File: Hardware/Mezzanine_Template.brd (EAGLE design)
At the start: 30.5 x 44.5 mm, 6 parts, among them U2 EDISON_CONNECTOR_FULLMOUNTING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, U3 EDISON_CONNECTOR_FULLHEADER

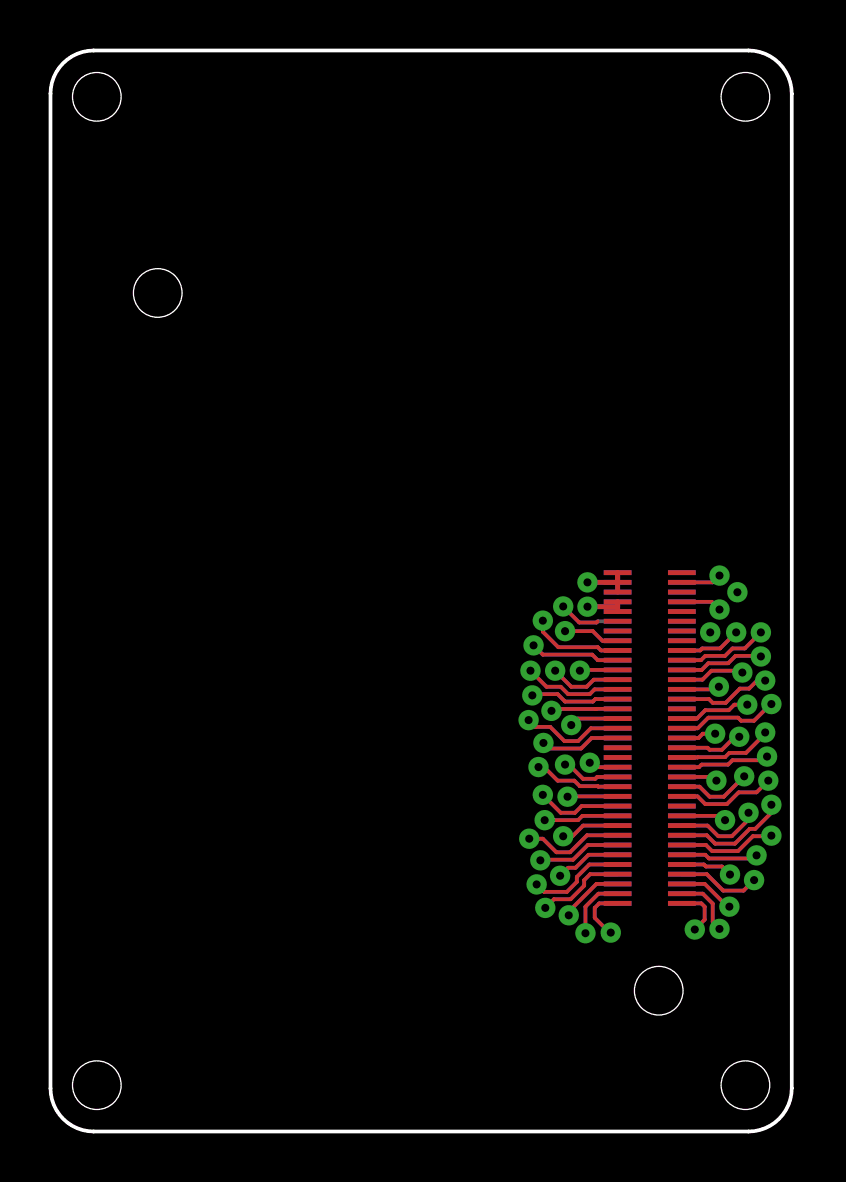
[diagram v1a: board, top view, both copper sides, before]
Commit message: added fiducials and second side logos to template
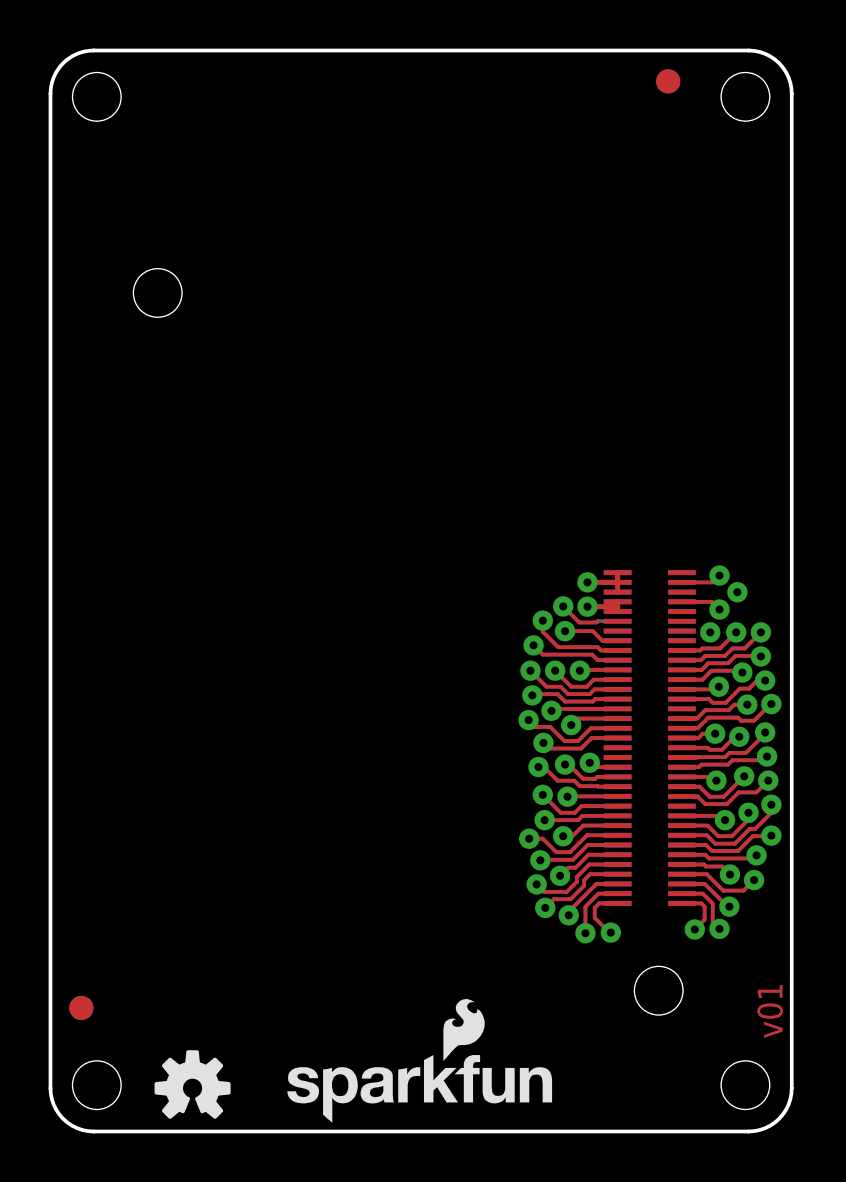
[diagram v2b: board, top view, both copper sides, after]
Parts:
- added FID1, FID2: FIDUCIAL1X2, SparkFun-Aesthetics:FIDUCIAL-1X2
- added LOGO1: OSHW-LOGOS, SparkFun-Aesthetics:OSHW-LOGO-S
- added LOGO4: SFE_LOGO_NAME_FLAME.1_INCH, SparkFun-Aesthetics:SFE_LOGO_NAME_FLAME_.1
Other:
- board text added: "v01"
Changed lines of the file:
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@@
 <dimension x1="29.28210625" y1="41.83789375" x2="27.86789375" y2="43.25210625" x3="34.29" y3="48.26" textsize="1.778" layer="51" dtype="diameter"/>
 <text x="29.21" y="6.35" size="1.016" layer="22" font="vector" ratio="15" rot="MR90" align="center">4xM2.0</text>
+<text x="30.099" y="3.81" size="1.016" layer="1" font="vector" ratio="14" rot="R90">v01</text>
 </plain>
 <attributes>
@@
 <element name="U3" library="Edison" package="DF40C-70DP-0.4(51)" value="EDISON_CONNECTOR_FULLHEADER" x="24.64" y="16.1798" rot="MR90"/>
 <element name="FRAME2" library="SparkFun-Aesthetics" package="CREATIVE_COMMONS" value="FRAME-LETTER" x="-1.27" y="-13.97"/>
+<element name="LOGO1" library="SparkFun-Aesthetics" package="OSHW-LOGO-S" value="OSHW-LOGOS" x="5.842" y="1.778"/>
+<element name="LOGO4" library="SparkFun-Aesthetics" package="SFE_LOGO_NAME_FLAME_.1" value="SFE_LOGO_NAME_FLAME.1_INCH" x="9.2964" y="0.254"/>
+<element name="FID1" library="SparkFun-Aesthetics" package="FIDUCIAL-1X2" value="FIDUCIAL1X2" x="1.27" y="5.08"/>
+<element name="FID2" library="SparkFun-Aesthetics" package="FIDUCIAL-1X2" value="FIDUCIAL1X2" x="25.4" y="43.18"/>
 </elements>
 <signals>
@@
 <contactref element="U2" pad="12"/>
 <contactref element="U3" pad="12"/>
-<wire x1="23.32" y1="20.9798" x2="23.32" y2="20.98" width="0" layer="19" extent="1-16"/>
+<wire x1="23.32" y1="20.98" x2="23.32" y2="20.9798" width="0" layer="19" extent="1-16"/>
 </signal>
 <signal name="FW_RCVR">

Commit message: - Added fiducials to both sides - flipped side name template is on - corrected 1.8v trace that was not connected. - removed my name from the designed by, Replaced with "Engineer" - Added template rev number to SCH.
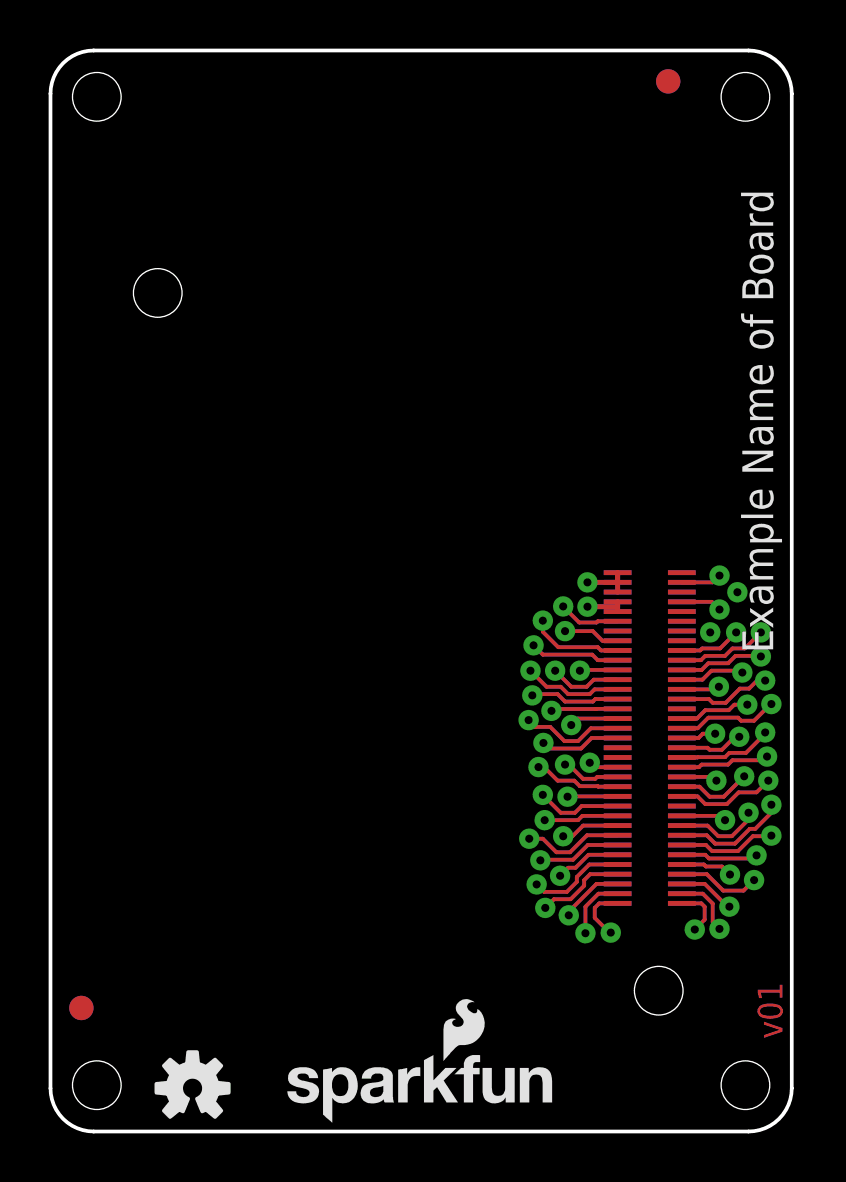
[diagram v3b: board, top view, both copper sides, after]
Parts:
- added FID3, FID4: FIDUCIAL1X2, SparkFun-Aesthetics:FIDUCIAL-1X2
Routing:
- net 1.8V: track 4.25 -> 5.07 mm
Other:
- board text added: "Engineer"
- board text removed: "Casey Kuhns"
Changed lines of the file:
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@@
 <wire x1="28.702" y1="0" x2="1.778" y2="0" width="0.1524" layer="20"/>
 <wire x1="0" y1="1.778" x2="0" y2="42.672" width="0.1524" layer="20"/>
-<text x="27.94" y="-13.97" size="1.6764" layer="51" ratio="15">Casey Kuhns</text>
+<text x="25.4" y="-13.97" size="1.6764" layer="51" ratio="15">Engineer</text>
 <hole x="28.575" y="1.905" drill="2"/>
 <hole x="1.905" y="1.905" drill="2"/>
@@
 <text x="-2.54" y="41.91" size="1.778" layer="51" rot="R270">LED's and selector switches go here</text>
 <text x="31.115" y="39.37" size="1.778" layer="51" rot="R270">Nothing goes here...  I mean it.</text>
-<text x="29.337" y="29.21" size="1.27" layer="22" font="vector" ratio="15" rot="MR90" align="center">Example Name of Board</text>
+<text x="29.083" y="29.21" size="1.27" layer="21" font="vector" ratio="15" rot="R90" align="center">Example Name of Board</text>
 <wire x1="1.778" y1="44.45" x2="28.702" y2="44.45" width="0.1524" layer="20"/>
 <wire x1="30.48" y1="44.704" x2="30.48" y2="53.34" width="0.254" layer="51"/>
@@
 <element name="FID1" library="SparkFun-Aesthetics" package="FIDUCIAL-1X2" value="FIDUCIAL1X2" x="1.27" y="5.08"/>
 <element name="FID2" library="SparkFun-Aesthetics" package="FIDUCIAL-1X2" value="FIDUCIAL1X2" x="25.4" y="43.18"/>
+<element name="FID3" library="SparkFun-Aesthetics" package="FIDUCIAL-1X2" value="FIDUCIAL1X2" x="1.27" y="5.08" rot="MR0"/>
+<element name="FID4" library="SparkFun-Aesthetics" package="FIDUCIAL-1X2" value="FIDUCIAL1X2" x="25.4" y="43.18" rot="MR0"/>
 </elements>
 <signals>
@@
 </signal>
 <signal name="1.8V">
-<wire x1="22.5038" y1="20.9798" x2="22.4536" y2="20.9296" width="0.1524" layer="1"/>
-<wire x1="22.4536" y1="20.9296" x2="21.7424" y2="20.9296" width="0.1524" layer="1"/>
-<wire x1="21.7424" y1="20.9296" x2="21.082" y2="21.59" width="0.1524" layer="1"/>
-<via x="21.082" y="21.59" extent="1-16" drill="0.3302"/>
 <wire x1="21.082" y1="21.59" x2="21.7424" y2="20.9296" width="0.1524" layer="16"/>
 <wire x1="21.7424" y1="20.9296" x2="22.4536" y2="20.9296" width="0.1524" layer="16"/>
@@
 <contactref element="U2" pad="12"/>
 <contactref element="U3" pad="12"/>
-<wire x1="23.32" y1="20.98" x2="23.32" y2="20.9798" width="0" layer="19" extent="1-16"/>
+<via x="21.082" y="21.59" extent="1-16" drill="0.3302"/>
+<wire x1="21.082" y1="21.59" x2="21.7424" y2="20.9296" width="0.1524" layer="1"/>
+<wire x1="21.7424" y1="20.9296" x2="22.4536" y2="20.9296" width="0.1524" layer="1"/>
+<wire x1="22.4536" y1="20.9296" x2="22.5044" y2="20.9804" width="0.1524" layer="1"/>
+<wire x1="22.5044" y1="20.9804" x2="23.3194" y2="20.9804" width="0.1524" layer="1"/>
+<wire x1="23.3194" y1="20.9804" x2="23.32" y2="20.9798" width="0.1524" layer="1"/>
 </signal>
 <signal name="FW_RCVR">

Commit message: corrected lables and removed extra packages that are no longer supported.
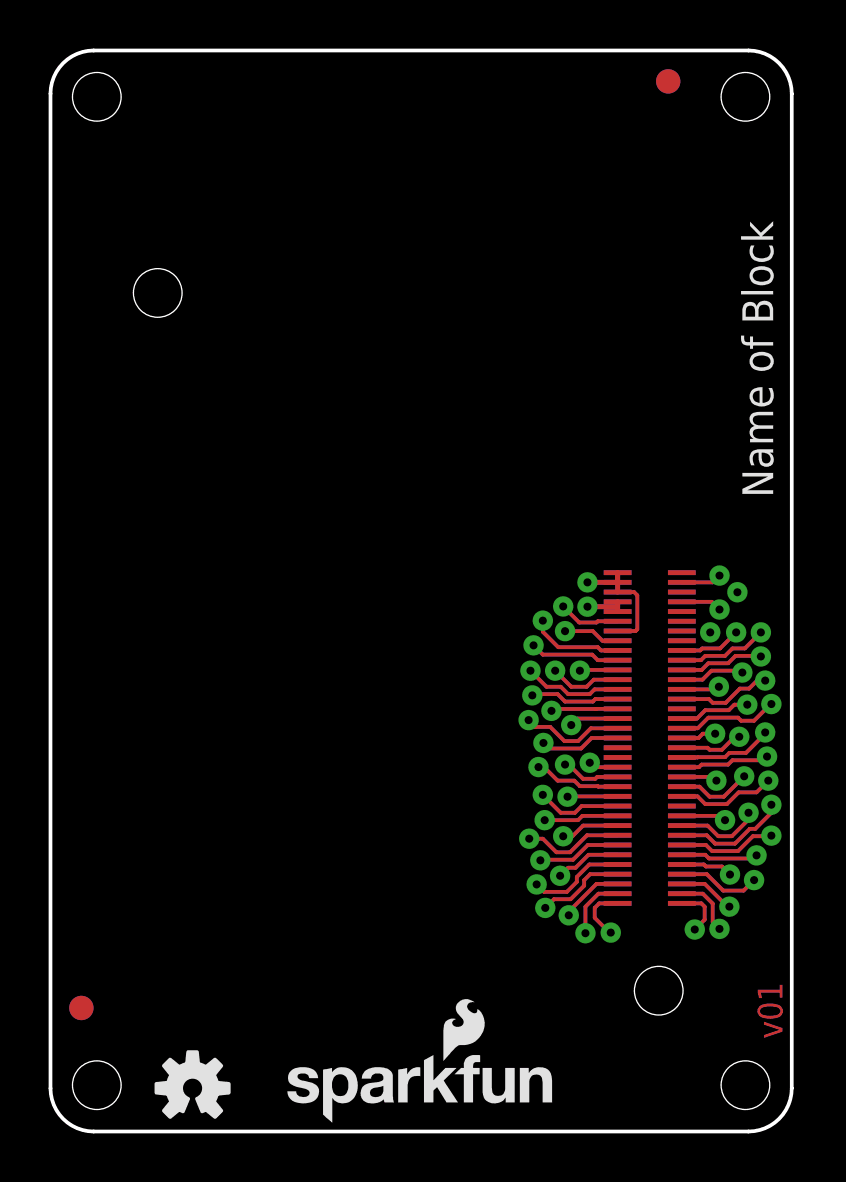
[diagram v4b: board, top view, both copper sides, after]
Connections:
- net VSYS: now also U2.14, U3.14
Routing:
- net VSYS: track 4.48 -> 10.7 mm
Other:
- board text added: "LED's & User Switches/Buttons Go Here"
- board text added: "Name of Block"
- board text added: "Note: Units are in Inches"
- board text added: "User Interface/ Connectors"
- board text removed: "Connectors Go Here"
- board text removed: "Example Name of Board"
- board text removed: "LED's and selector switches go here"
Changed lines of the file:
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@@
 <?xml version="1.0" encoding="utf-8"?>
 <!DOCTYPE eagle SYSTEM "eagle.dtd">
-<eagle version="6.5.0">
+<eagle version="6.6.0">
 <drawing>
 <settings>
@@
 <setting verticaltext="up"/>
 </settings>
-<grid distance="0.05" unitdist="inch" unit="inch" style="lines" multiple="1" display="yes" altdistance="0.005" altunitdist="inch" altunit="inch"/>
+<grid distance="0.001" unitdist="inch" unit="inch" style="lines" multiple="1" display="yes" altdistance="0.005" altunitdist="inch" altunit="inch"/>
 <layers>
 <layer number="1" name="Top" color="4" fill="1" visible="yes" active="yes"/>
@@
 <layer number="20" name="Dimension" color="15" fill="1" visible="yes" active="yes"/>
 <layer number="21" name="tPlace" color="16" fill="1" visible="yes" active="yes"/>
-<layer number="22" name="bPlace" color="14" fill="1" visible="yes" active="yes"/>
+<layer number="22" name="bPlace" color="14" fill="1" visible="no" active="yes"/>
 <layer number="23" name="tOrigins" color="15" fill="1" visible="yes" active="yes"/>
 <layer number="24" name="bOrigins" color="15" fill="1" visible="yes" active="yes"/>
@@
 <hole x="1.905" y="42.545" drill="2"/>
 <hole x="28.575" y="42.545" drill="2"/>
-<text x="4.445" y="45.085" size="1.778" layer="51">Connectors Go Here</text>
-<text x="-2.54" y="41.91" size="1.778" layer="51" rot="R270">LED's and selector switches go here</text>
+<text x="8.255" y="45.085" size="1.778" layer="51">User Interface/
+ Connectors</text>
+<text x="-2.54" y="41.91" size="1.778" layer="51" rot="R270">LED's &amp; User Switches/Buttons Go Here</text>
 <text x="31.115" y="39.37" size="1.778" layer="51" rot="R270">Nothing goes here...  I mean it.</text>
-<text x="29.083" y="29.21" size="1.27" layer="21" font="vector" ratio="15" rot="R90" align="center">Example Name of Board</text>
+<text x="29.083" y="31.75" size="1.27" layer="21" font="vector" ratio="15" rot="R90" align="center">Name of Block</text>
 <wire x1="1.778" y1="44.45" x2="28.702" y2="44.45" width="0.1524" layer="20"/>
 <wire x1="30.48" y1="44.704" x2="30.48" y2="53.34" width="0.254" layer="51"/>
@@
 <rectangle x1="22.098" y1="26.162" x2="30.48" y2="44.45" layer="42" rot="R180"/>
 <rectangle x1="22.098" y1="26.162" x2="30.48" y2="44.45" layer="41" rot="R180"/>
-<dimension x1="1.778" y1="42.672" x2="0.4190875" y2="43.81858125" x3="-5.542384375" y3="48.848575" textsize="1.778" layer="51" dtype="radius"/>
+<dimension x1="1.905" y1="42.545" x2="0.4190875" y2="43.81858125" x3="-5.503225" y3="48.894621875" textsize="1.778" layer="51" dtype="radius" unit="inch"/>
 <dimension x1="29.28210625" y1="41.83789375" x2="27.86789375" y2="43.25210625" x3="34.29" y3="48.26" textsize="1.778" layer="51" dtype="diameter"/>
 <text x="29.21" y="6.35" size="1.016" layer="22" font="vector" ratio="15" rot="MR90" align="center">4xM2.0</text>
-<text x="30.099" y="3.81" size="1.016" layer="1" font="vector" ratio="14" rot="R90">v01</text>
+<text x="30.099" y="3.81" size="1.016" layer="1" font="vector" ratio="15" rot="R90">v01</text>
+<text x="33.02" y="-3.81" size="1.778" layer="51">Note: Units are in Inches</text>
+<text x="29.083" y="31.75" size="1.27" layer="22" font="vector" ratio="15" rot="SMR270" align="center">Name of Block</text>
 </plain>
 <attributes>
@@
 <signals>
 <signal name="GND">
-<polygon width="0.1778" layer="16" spacing="0.254" isolate="0.1524" orphans="yes" rank="6">
+<polygon width="0.1778" layer="16" spacing="0.254" orphans="yes" rank="6">
 <vertex x="30.48" y="42.672"/>
 <vertex x="30.48" y="1.778" curve="-90"/>
@@
 <contactref element="U3" pad="2"/>
 <contactref element="U3" pad="4"/>
+<contactref element="U2" pad="14"/>
+<contactref element="U3" pad="14"/>
+<wire x1="23.32" y1="22.1798" x2="23.9974" y2="22.1798" width="0.1524" layer="1"/>
+<wire x1="23.9974" y1="22.1798" x2="24.13" y2="22.0472" width="0.1524" layer="1"/>
+<wire x1="24.13" y1="22.0472" x2="24.13" y2="20.6502" width="0.1524" layer="1"/>
+<wire x1="24.13" y1="20.6502" x2="24.0596" y2="20.5798" width="0.1524" layer="1"/>
+<wire x1="24.0596" y1="20.5798" x2="23.32" y2="20.5798" width="0.1524" layer="1"/>
+<wire x1="23.32" y1="20.58" x2="24.0598" y2="20.58" width="0.1524" layer="16"/>
+<wire x1="24.0598" y1="20.58" x2="24.13" y2="20.6502" width="0.1524" layer="16"/>
+<wire x1="24.13" y1="20.6502" x2="24.13" y2="22.0472" width="0.1524" layer="16"/>
+<wire x1="24.13" y1="22.0472" x2="23.9974" y2="22.1798" width="0.1524" layer="16"/>
+<wire x1="23.9974" y1="22.1798" x2="23.3202" y2="22.1798" width="0.1524" layer="16"/>
+<wire x1="23.3202" y1="22.1798" x2="23.32" y2="22.18" width="0.1524" layer="16"/>
 </signal>
 <signal name="3.3V">
@@
 <wire x1="21.7424" y1="20.9296" x2="22.4536" y2="20.9296" width="0.1524" layer="16"/>
 <wire x1="22.4536" y1="20.9296" x2="22.504" y2="20.98" width="0.1524" layer="16"/>
-<wire x1="22.504" y1="20.98" x2="23.32" y2="20.98" width="0.1524" layer="16"/>
 <contactref element="U2" pad="12"/>
 <contactref element="U3" pad="12"/>
@@
 <wire x1="22.5044" y1="20.9804" x2="23.3194" y2="20.9804" width="0.1524" layer="1"/>
 <wire x1="23.3194" y1="20.9804" x2="23.32" y2="20.9798" width="0.1524" layer="1"/>
+<wire x1="22.504" y1="20.98" x2="23.32" y2="20.98" width="0.1524" layer="16"/>
 </signal>
 <signal name="FW_RCVR">
@@
 </board>
 </drawing>
+<compatibility>
+<note version="6.3" minversion="6.2.2" severity="warning">
+Since Version 6.2.2 text objects can contain more than one line,
+which will not be processed correctly with this version.
+</note>
+</compatibility>
 </eagle>
